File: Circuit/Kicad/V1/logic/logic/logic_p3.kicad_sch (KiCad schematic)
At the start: 0 parts

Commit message: version1.2.1のLogic周りの回路図を書いた
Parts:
- added C10_Bypass?, C14_Bypass?, C1_Bypass?, C5_Bypass?: C_0.1uF, symbol Device:C_Small
- added C11_Decupling, C15_Decupling?, C18_Decupling, C2_Decupling, C6_Decupling?, C9_Decupling: C_10uF, symbol Device:C_Small
- added C12_Decupling?, C17_Decupling?, C3_Decupling?, C8_Decupling?: C_1uF, symbol Device:C_Small
- added C13_Bypass, C16_Bypass, C1_Bypass, C7_Bypass: C_10nF, symbol Device:C_Small
- added FB1 (x2), FB10, FB3, FB4, FB5, FB6, FB7, FB8, FB9: FerriteBead, symbol Device:FerriteBead_Small
- added Left-Leg, Left_Leg: ISOW1044, symbol CAN_Transceiver:ISOW1044
- added R1, R3: R_4.7k, symbol Device:R
- added R2_TERM, R4_TERM: R_120, symbol Device:R
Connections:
- new net: C16_Bypass.1, C17_Decupling?.1, C18_Decupling.1, FB9.1, Left_Leg.12 (V_{ISOOUT}), Left_Leg.13 (V_{SIN})
- new net: C16_Bypass.2, C17_Decupling?.2, C18_Decupling.2, FB10.1, Left_Leg.11 (GND2)
- new net: C1_Bypass?.1, FB1.2, Left-Leg.1 (V_{IO}), R1.2
- new net: Left_Leg.8 (EN/FLT), R3.1
- new net: C10_Bypass?.1, FB6.2, Left_Leg.1 (V_{IO}), R3.2
- new net: C5_Bypass?.1, C6_Decupling?.1, FB4.2, Left-Leg.20 (V_{ISOIN})
- new net: C11_Decupling.1, C12_Decupling?.1, C13_Bypass.1, FB7.2, Left_Leg.9 (V_{DD})
- new net: C7_Bypass.2, C8_Decupling?.2, C9_Decupling.2, FB5.1, Left-Leg.11 (GND2)
- new net: C14_Bypass?.1, C15_Decupling?.1, FB9.2, Left_Leg.20 (V_{ISOIN})
- new net: C1_Bypass.1, C2_Decupling.1, C3_Decupling?.1, FB1.2, Left-Leg.9 (V_{DD})
- new net: C7_Bypass.1, C8_Decupling?.1, C9_Decupling.1, FB4.1, Left-Leg.12 (V_{ISOOUT}), Left-Leg.13 (V_{SIN})
- new net: Left-Leg.8 (EN/FLT), R1.1
- new net +5V: FB1.1, FB1.1, FB6.1, FB7.1
- new net B: Left-Leg.2 (IN)
- new net C: Left-Leg.4 (STB)
- new net CAN1_H: Left-Leg.19 (CANH), R2_TERM.1
- new net CAN1_L: Left-Leg.18 (CANL), R2_TERM.2
- new net CAN1_RX: Left-Leg.5 (RXD)
- new net CAN1_TX: Left-Leg.3 (TXD)
- new net CAN2_H: Left_Leg.19 (CANH), R4_TERM.1
- new net CAN2_L: Left_Leg.18 (CANL), R4_TERM.2
- new net CAN2_RX: Left_Leg.5 (RXD)
- new net CAN2_TX: Left_Leg.3 (TXD)
- new net D: Left_Leg.2 (IN)
- new net E: Left_Leg.4 (STB)
- new net GND: C10_Bypass?.2, C11_Decupling.2, C12_Decupling?.2, C13_Bypass.2, C1_Bypass.2, C1_Bypass?.2, C2_Decupling.2, C3_Decupling?.2, FB3.1, FB3.2, FB8.1, FB8.2, Left-Leg.10 (GND1), Left-Leg.6 (GNDIO), Left_Leg.10 (GND1), Left_Leg.6 (GNDIO)
- new net GND1: C14_Bypass?.2, C15_Decupling?.2, C5_Bypass?.2, C6_Decupling?.2, FB10.2, FB5.2, Left-Leg.15 (GISOIN), Left-Leg.16 (GISOIN), Left-Leg.17 (GISOIN), Left_Leg.15 (GISOIN), Left_Leg.16 (GISOIN), Left_Leg.17 (GISOIN)
- no-connect marks 0 -> 4
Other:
- note added: "Logic_GND"
- note added: "Power_GND"
- note added: "from/to_STM32"

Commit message: footprintを一部追加
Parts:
- renumbered C1_Bypass to C4_Bypass, FB1 to FB2, Left-Leg to Right-Leg
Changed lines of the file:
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@@
   (symbol (lib_id "Device:FerriteBead_Small") (at 27.94 101.6 90) (unit 1)
     (in_bom yes) (on_board yes) (fields_autoplaced)
-    (property "Reference" "FB1" (id 0) (at 27.9019 95.25 90))
+    (property "Reference" "FB2" (id 0) (at 27.9019 95.25 90))
     (property "Value" "FerriteBead" (id 1) (at 27.9019 97.79 90))
     (property "Footprint" "" (id 2) (at 27.94 103.378 90)
@@
   (symbol (lib_id "Device:C_Small") (at 55.88 104.14 0) (unit 1)
     (in_bom yes) (on_board yes)
-    (property "Reference" "C1_Bypass" (id 0) (at 50.8 119.38 0)
+    (property "Reference" "C4_Bypass" (id 0) (at 50.8 119.38 0)
       (effects (font (size 1.27 1.27)) (justify left))
     )
@@
   (symbol (lib_name "ISOW1044_1") (lib_id "CAN_Transceiver:ISOW1044") (at 80.01 81.28 0) (unit 1)
     (in_bom yes) (on_board yes) (fields_autoplaced)
-    (property "Reference" "Left-Leg" (id 0) (at 80.01 73.66 0))
+    (property "Reference" "Right-Leg" (id 0) (at 80.01 73.66 0))
     (property "Value" "ISOW1044" (id 1) (at 80.01 76.2 0))
     (property "Footprint" "" (id 2) (at 74.93 81.28 0)

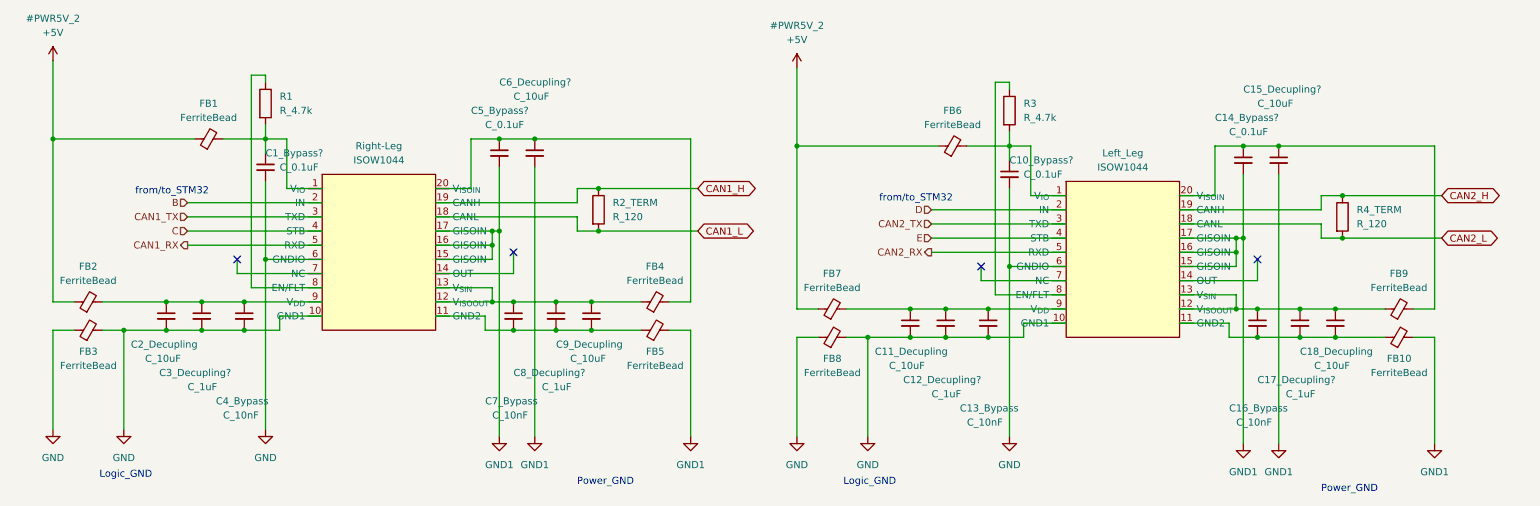
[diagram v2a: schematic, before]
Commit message: LogicのPCBを途中まで作った
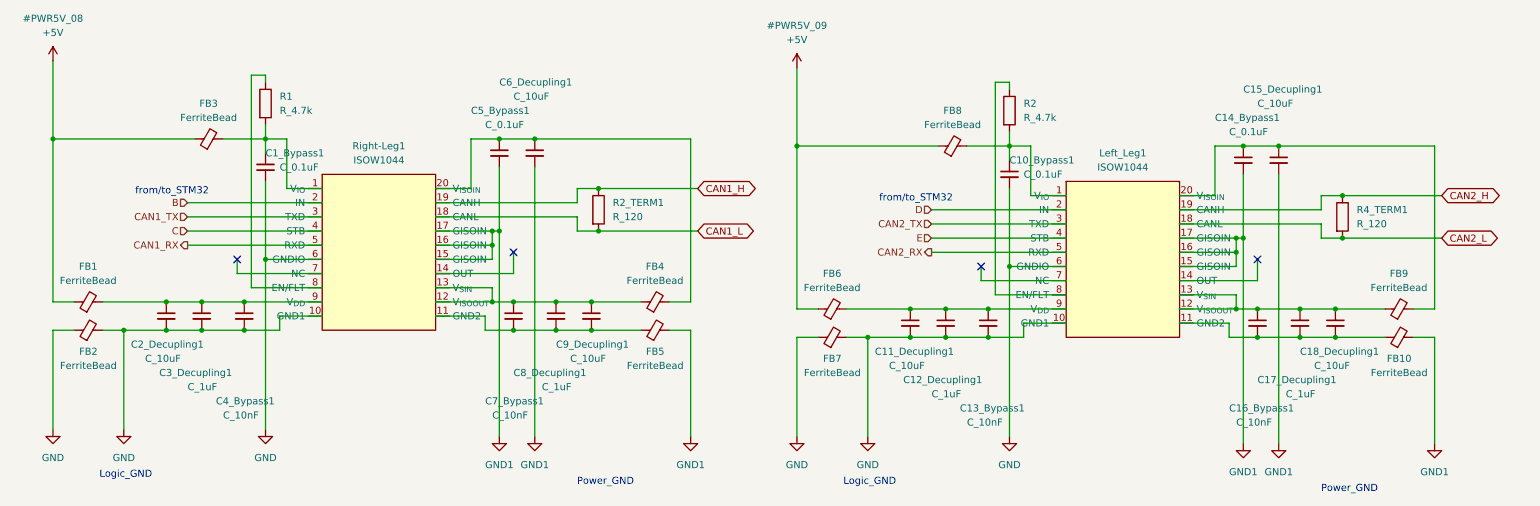
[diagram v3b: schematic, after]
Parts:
- C10_Bypass1: renamed from C10_Bypass?; footprint (none) -> CAN_Pheripheral:GRM188F11H104ZA01
- C11_Decupling1: renamed from C11_Decupling; footprint (none) -> CAN_Pheripheral:GRM188R6YA106MA73
- C12_Decupling1: renamed from C12_Decupling?; footprint (none) -> CAN_Pheripheral:GRM188B31H105KAAL
- C13_Bypass1: renamed from C13_Bypass; footprint (none) -> CAN_Pheripheral:GRM188B11H103KA01
- C14_Bypass1: renamed from C14_Bypass?; footprint (none) -> CAN_Pheripheral:GRM188F11H104ZA01
- C15_Decupling1: renamed from C15_Decupling?; footprint (none) -> CAN_Pheripheral:GRM188R6YA106MA73
- C16_Bypass1: renamed from C16_Bypass; footprint (none) -> CAN_Pheripheral:GRM188B11H103KA01
- C17_Decupling1: renamed from C17_Decupling?; footprint (none) -> CAN_Pheripheral:GRM188B31H105KAAL
- C18_Decupling1: renamed from C18_Decupling; footprint (none) -> CAN_Pheripheral:GRM188R6YA106MA73
- C1_Bypass1: renamed from C1_Bypass?; footprint (none) -> CAN_Pheripheral:GRM188F11H104ZA01
- C2_Decupling1: renamed from C2_Decupling; footprint (none) -> CAN_Pheripheral:GRM188R6YA106MA73
- C3_Decupling1: renamed from C3_Decupling?; footprint (none) -> CAN_Pheripheral:GRM188B31H105KAAL
- C4_Bypass1: renamed from C4_Bypass; footprint (none) -> CAN_Pheripheral:GRM188B11H103KA01
- C5_Bypass1: renamed from C5_Bypass?; footprint (none) -> CAN_Pheripheral:GRM188F11H104ZA01
- C6_Decupling1: renamed from C6_Decupling?; footprint (none) -> CAN_Pheripheral:GRM188R6YA106MA73
- C7_Bypass1: renamed from C7_Bypass; footprint (none) -> CAN_Pheripheral:GRM188B11H103KA01
- C8_Decupling1: renamed from C8_Decupling?; footprint (none) -> CAN_Pheripheral:GRM188B31H105KAAL
- C9_Decupling1: renamed from C9_Decupling; footprint (none) -> CAN_Pheripheral:GRM188R6YA106MA73
- FB1: renamed from FB2; footprint (none) -> CAN_Pheripheral:BLM21PG331SN
- FB10, FB4, FB5, FB9: footprint (none) -> CAN_Pheripheral:BLM21PG331SN
- FB2: renamed from FB3; footprint (none) -> CAN_Pheripheral:BLM21PG331SN
- FB3: renamed from FB1; footprint (none) -> CAN_Pheripheral:BLM21PG331SN
- FB6: renamed from FB7; footprint (none) -> CAN_Pheripheral:BLM21PG331SN
- FB7: renamed from FB8; footprint (none) -> CAN_Pheripheral:BLM21PG331SN
- FB8: renamed from FB6; footprint (none) -> CAN_Pheripheral:BLM21PG331SN
- Left_Leg1: renamed from Left_Leg; footprint (none) -> CAN_Transceiver:ISOW1044BDFMR
- R1: footprint (none) -> CAN_Pheripheral:RK73B2ATTD472J
- R2: renamed from R3; footprint (none) -> CAN_Pheripheral:RK73B2ATTD472J
- R2_TERM1: renamed from R2_TERM; footprint (none) -> CAN_Pheripheral:RK73B2ATTD121J
- R4_TERM1: renamed from R4_TERM; footprint (none) -> CAN_Pheripheral:RK73B2ATTD121J
- Right-Leg1: renamed from Right-Leg; footprint (none) -> CAN_Transceiver:ISOW1044BDFMR

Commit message: can回路にLEDを追加。整理。
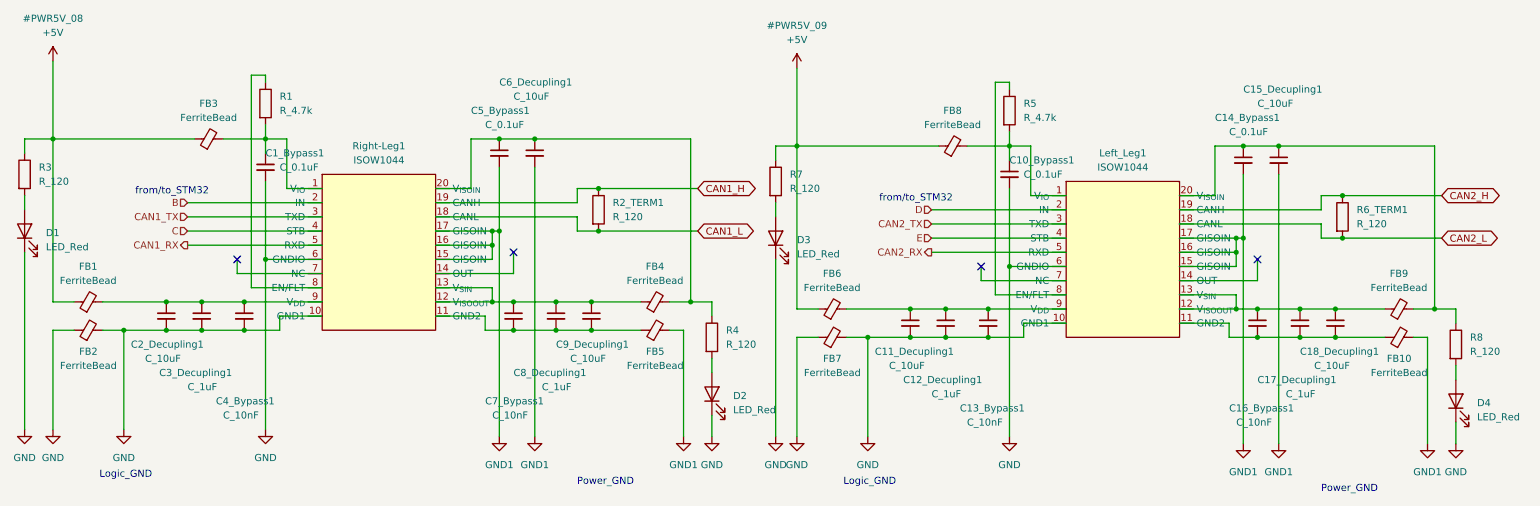
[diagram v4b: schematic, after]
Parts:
- added D1, D2, D3, D4: LED_Red, symbol Device:LED
- added R3, R4, R7, R8: R_120, symbol Device:R
- renumbered R2 to R5, R4_TERM1 to R6_TERM1
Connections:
- net +5V: now also R3.1, R7.1
- net GND: now also D1.1 (K), D2.1 (K), D3.1 (K), D4.1 (K)
- net at C5_Bypass1.1, C6_Decupling1.1, FB4.2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: now also R4.1
- net at C14_Bypass1.1, C15_Decupling1.1, FB9.2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: now also R8.1
- new net: D1.2 (A), R3.2
- new net: D3.2 (A), R7.2
- new net: D2.2 (A), R4.2
- new net: D4.2 (A), R8.2

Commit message: Version1のLogic基板が、形はできた。検査や見積もりはまだ
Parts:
- R3, R4, R7, R8: value R_120 -> R_1k
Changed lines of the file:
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@@
       (effects (font (size 1.27 1.27)) (justify left))
     )
-    (property "Value" "R_120" (id 1) (at 19.05 80.0099 0)
+    (property "Value" "R_1k" (id 1) (at 19.05 80.0099 0)
       (effects (font (size 1.27 1.27)) (justify left))
     )
@@
       (effects (font (size 1.27 1.27)) (justify left))
     )
-    (property "Value" "R_120" (id 1) (at 275.59 110.4899 0)
+    (property "Value" "R_1k" (id 1) (at 275.59 110.4899 0)
       (effects (font (size 1.27 1.27)) (justify left))
     )
@@
       (effects (font (size 1.27 1.27)) (justify left))
     )
-    (property "Value" "R_120" (id 1) (at 142.24 109.2199 0)
+    (property "Value" "R_1k" (id 1) (at 142.24 109.2199 0)
       (effects (font (size 1.27 1.27)) (justify left))
     )
@@
       (effects (font (size 1.27 1.27)) (justify left))
     )
-    (property "Value" "R_120" (id 1) (at 153.67 81.2799 0)
-      (effects (font (size 1.27 1.27)) (justify left))
-    )
+    (property "Value" "R_1k" (id 1) (at 153.67 81.2799 0)
+      (effects (font (size 1.27 1.27)) (justify left))
+    )
